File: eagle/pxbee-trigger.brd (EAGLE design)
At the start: 51 x 57 mm, 21 parts, among them J1 39501-1002, J2 39501-1009, K1 APAN3103, K2 APAN3103, K3 APAN3103, K4 APAN3103, Q1 BC548BTA, Q2 BC548BTA, Q3 BC548BTA, Q4 BC548BTA

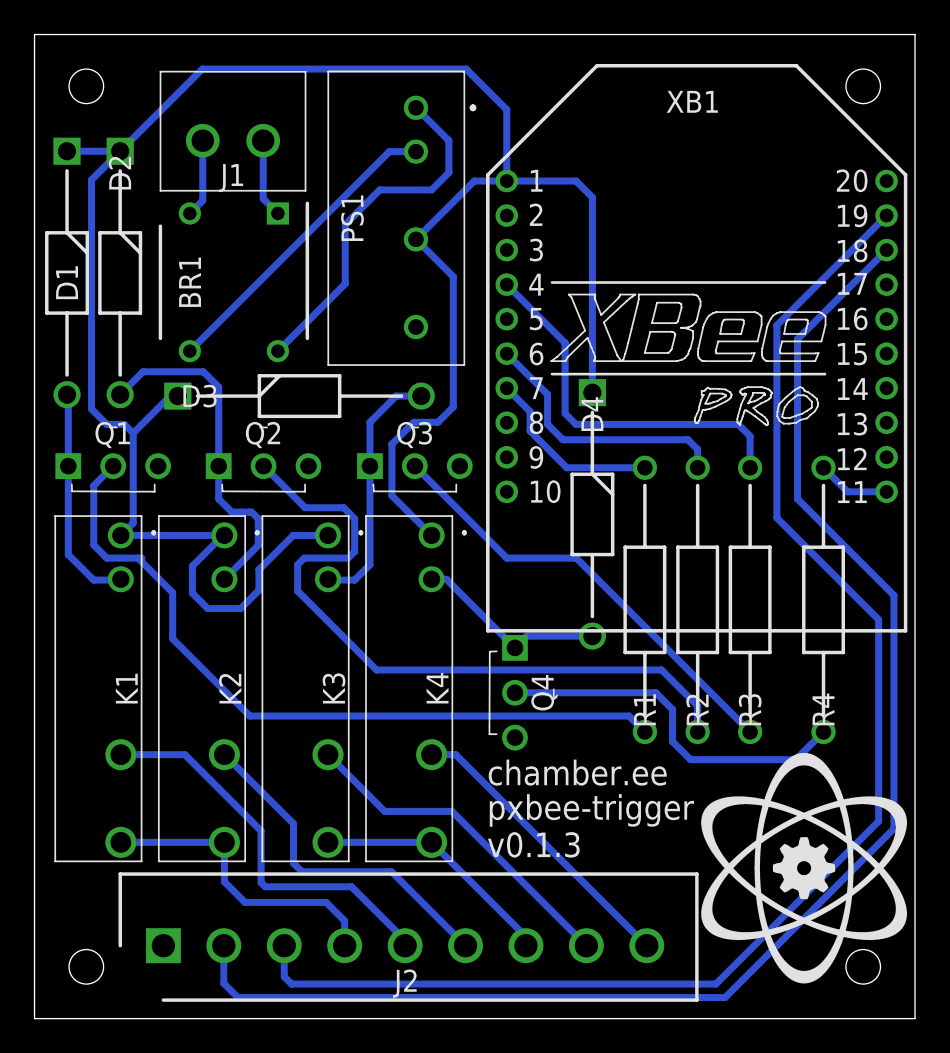
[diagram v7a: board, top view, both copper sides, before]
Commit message: PCB layout fine tuning and fabrication prep
- Addresses findings in #6
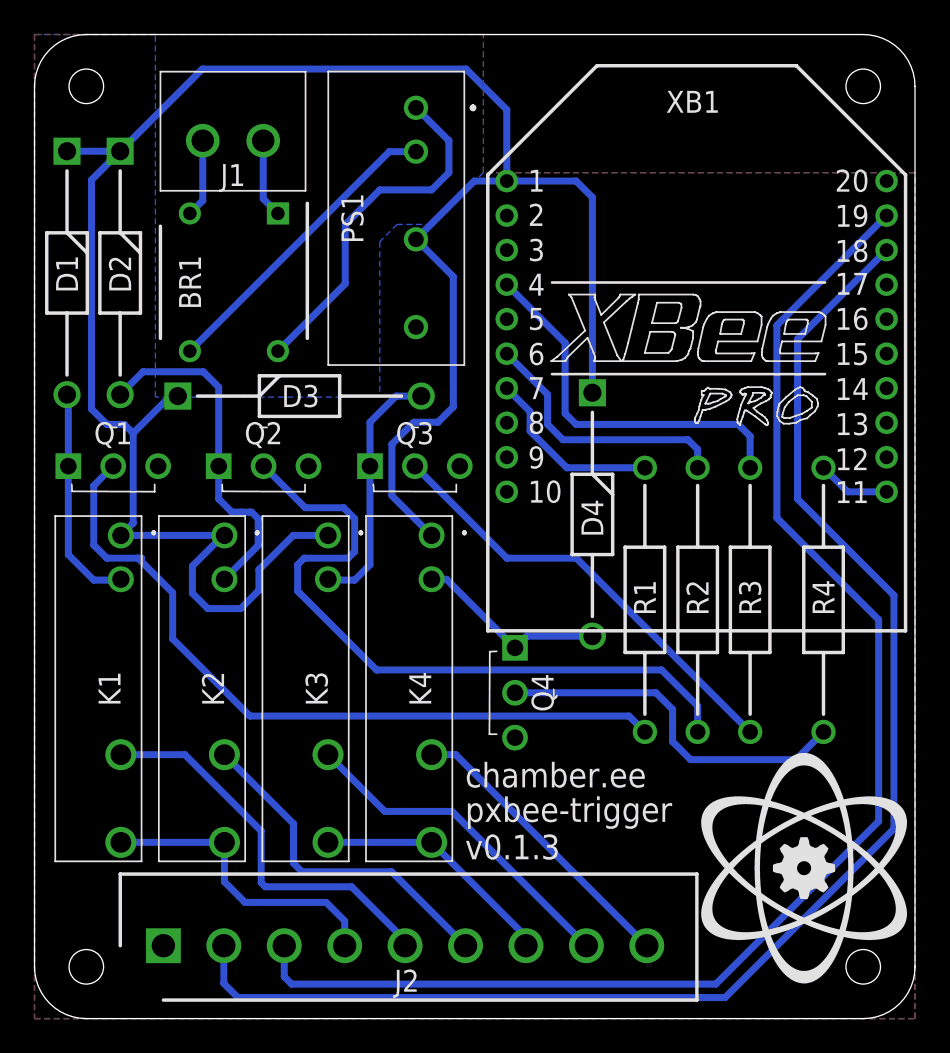
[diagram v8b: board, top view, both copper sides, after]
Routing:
- added copper zone on layer 1, net GND
- added copper zone on layer 16, net GND
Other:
- outline, holes or cut-outs redrawn
